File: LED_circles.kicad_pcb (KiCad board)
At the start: 2 copper layers, 125 x 125 mm, 134 parts, among them J1 Conn_ARM_SWD_EDGE, J2 USB4125-GF-A, U74 BD33GA3WEFJ, U75 M95256-WMN6P, U76 M95256-WMN6P, U77 STM32G071KBTxN

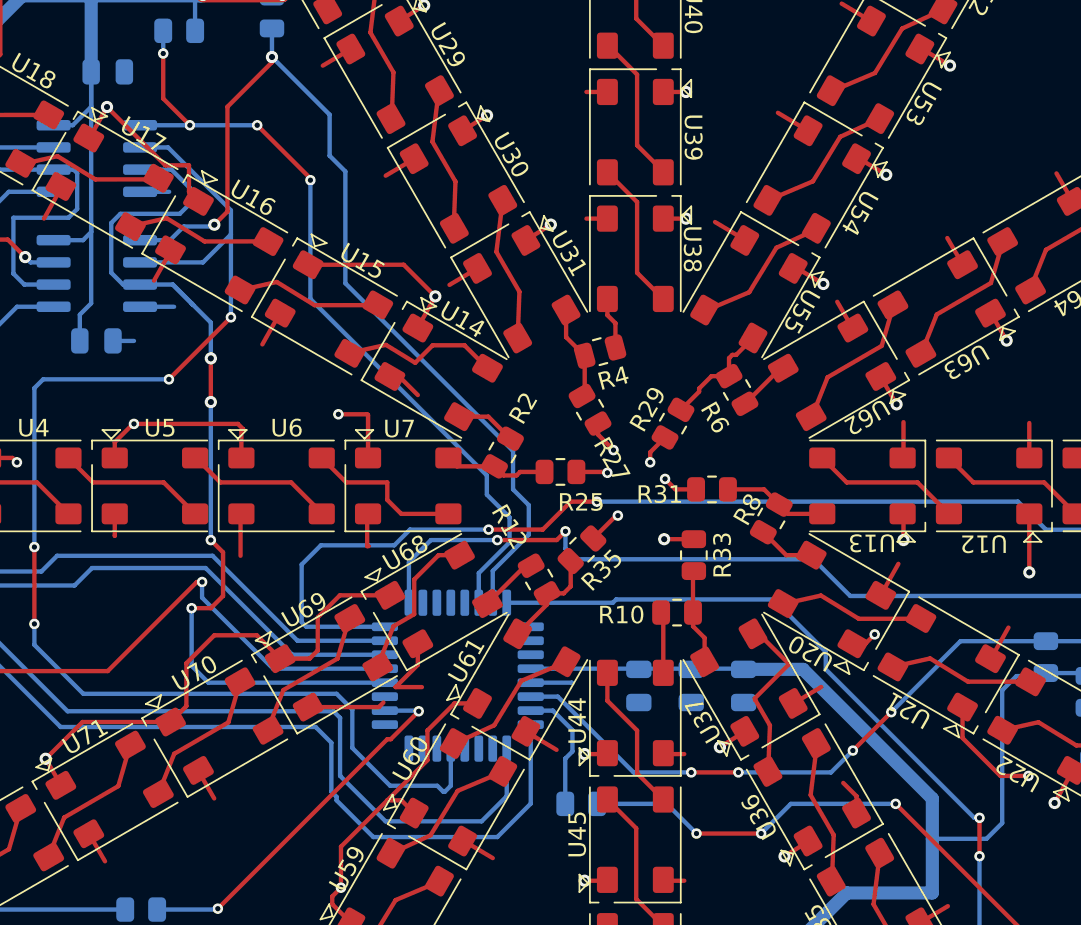
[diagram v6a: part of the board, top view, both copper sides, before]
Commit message: Fixed DRC issues
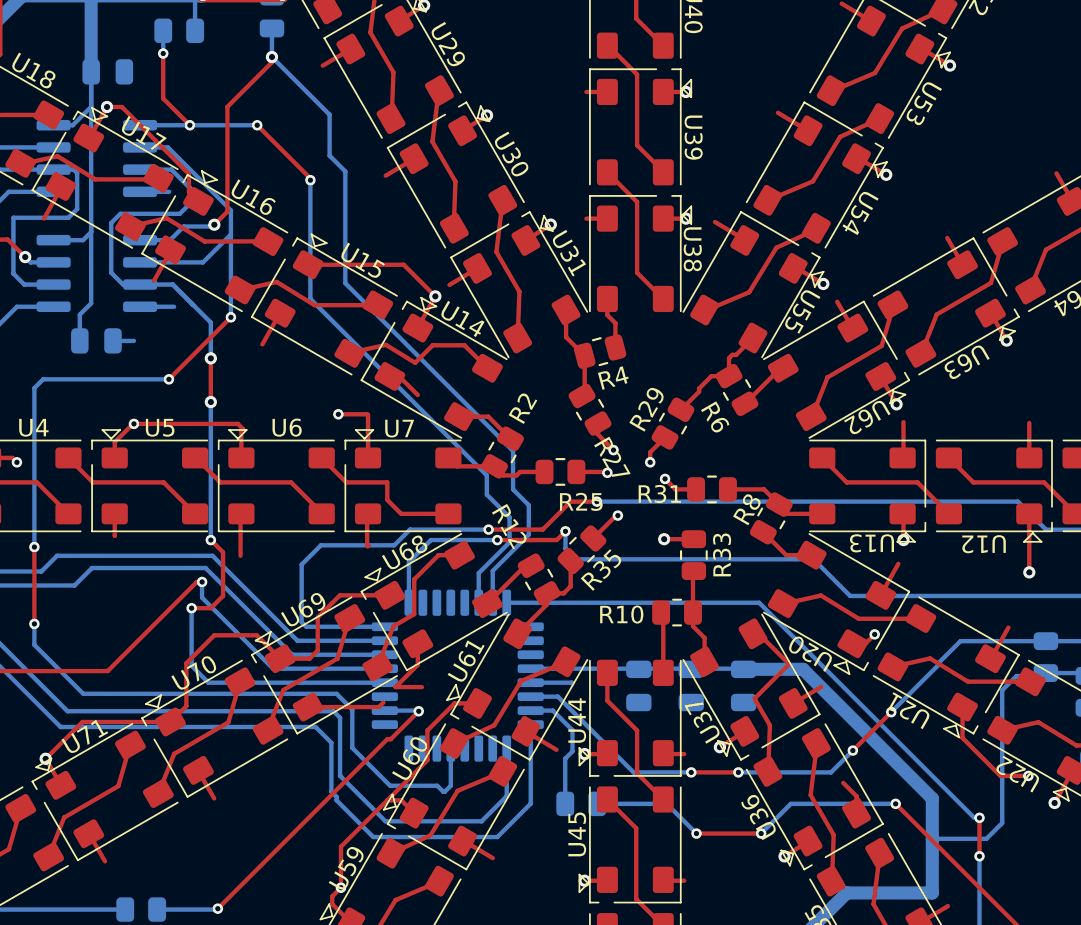
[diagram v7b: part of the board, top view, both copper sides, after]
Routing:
- net Net-(D1-A): track 106.8 -> 106.0 mm
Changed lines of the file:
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@@
-	)
-	(segment
-		(start 117.95 83.171916)
-		(end 117.95 81.65)
-		(width 0.25)
-		(layer "F.Cu")
-		(net 62)
 	)
 	(segment
@@
 	)
 	(segment
-		(start 116.595749 81.65)
-		(end 113.256391 78.310642)
-		(width 0.25)
-		(layer "F.Cu")
-		(net 62)
-	)
-	(segment
 		(start 160.628717 132.85)
 		(end 159.189358 133.756391)
@@
 	)
 	(segment
+		(start 113.256391 78.310642)
+		(end 114.110642 78.310642)
+		(width 0.25)
+		(layer "F.Cu")
+		(net 62)
+	)
+	(segment
 		(start 124.850642 109.889358)
 		(end 125.32 109.42)
@@
 	)
 	(segment
-		(start 118.492444 83.71436)
-		(end 117.95 83.171916)
-		(width 0.25)
-		(layer "F.Cu")
-		(net 62)
-	)
-	(segment
 		(start 99.2 98.4)
 		(end 99.2 96.55)
@@
 	)
 	(segment
-		(start 117.95 81.65)
-		(end 116.595749 81.65)
-		(width 0.25)
-		(layer "F.Cu")
-		(net 62)
-	)
-	(segment
 		(start 141.9 122.6)
 		(end 140.6 122.6)
@@
 	)
 	(segment
+		(start 117.95 83.171916)
+		(end 118.492444 83.71436)
+		(width 0.25)
+		(layer "F.Cu")
+		(net 62)
+	)
+	(segment
 		(start 141.85 99.2)
 		(end 141.9 99.25)
@@
 	)
 	(segment
+		(start 114.110642 78.310642)
+		(end 117.95 82.15)
+		(width 0.25)
+		(layer "F.Cu")
+		(net 62)
+	)
+	(segment
 		(start 145.1 84.7)
 		(end 146.4 84.7)
@@
 		(start 145.15 70.2)
 		(end 146.45 70.2)
+		(width 0.25)
+		(layer "F.Cu")
+		(net 62)
+	)
+	(segment
+		(start 117.95 82.15)
+		(end 117.95 83.171916)
 		(width 0.25)
 		(layer "F.Cu")
@@
 	)
 	(segment
-		(start 154.4 109.5)
-		(end 154.4 110.5)
+		(start 123 147.5)
+		(end 117.5 153)
+		(width 0.25)
+		(layer "B.Cu")
+		(net 63)
+	)
+	(segment
+		(start 118 157.5)
+		(end 118.05 157.55)
+		(width 0.25)
+		(layer "B.Cu")
+		(net 63)
+	)
+	(segment
+		(start 163.2 121.2)
+		(end 163.2 126.1)
+		(width 0.25)
+		(layer "B.Cu")
+		(net 63)
+	)
+	(segment
+		(start 118.05 157.55)
+		(end 121.4 157.55)
+		(width 0.25)
+		(layer "B.Cu")
+		(net 63)
+	)
+	(segment
+		(start 162.4 126.9)
+		(end 157.15056 126.9)
+		(width 0.25)
+		(layer "B.Cu")
+		(net 63)
+	)
+	(segment
+		(start 150.58795 106.68795)
+		(end 162.9 119)
+		(width 0.25)
+		(layer "B.Cu")
+		(net 63)
+	)
+	(segment
+		(start 163.2 126.1)
+		(end 162.4 126.9)
+		(width 0.25)
+		(layer "B.Cu")
+		(net 63)
+	)
+	(segment
+		(start 118 157)
+		(end 118 157.5)
+		(width 0.25)
+		(layer "B.Cu")
+		(net 63)
+	)
+	(segment
+		(start 117.5 156.5)
+		(end 118 157)
+		(width 0.25)
+		(layer "B.Cu")
+		(net 63)
+	)
+	(segment
+		(start 136.137104 106.68795)
+		(end 150.58795 106.68795)
 		(width 0.25)
 		(layer "B.Cu")
@@
 		(width 0.25)
 		(layer "B.Cu")
-		(net 63)
-	)
-	(segment
-		(start 142.4 106.5)
-		(end 151.4 106.5)
-		(width 0.25)
-		(layer "B.Cu")
-		(net 63)
-	)
-	(segment
-		(start 151.4 106.5)
-		(end 154.4 109.5)
-		(width 0.25)
-		(layer "B.Cu")
-		(net 63)
-	)
-	(segment
-		(start 123 147.5)
-		(end 117.5 153)
-		(width 0.25)
-		(layer "B.Cu")
-		(net 63)
-	)
-	(segment
-		(start 118 157.5)
-		(end 118.05 157.55)
-		(width 0.25)
-		(layer "B.Cu")
-		(net 63)
-	)
-	(segment
-		(start 136.137104 106.68795)
-		(end 142.21205 106.68795)
-		(width 0.25)
-		(layer "B.Cu")
-		(net 63)
-	)
-	(segment
-		(start 163.2 121.2)
-		(end 163.2 126.1)
-		(width 0.25)
-		(layer "B.Cu")
-		(net 63)
-	)
-	(segment
-		(start 118.05 157.55)
-		(end 121.4 157.55)
-		(width 0.25)
-		(layer "B.Cu")
-		(net 63)
-	)
-	(segment
-		(start 162.4 126.9)
-		(end 157.15056 126.9)
-		(width 0.25)
-		(layer "B.Cu")
-		(net 63)
-	)
-	(segment
-		(start 163.2 126.1)
-		(end 162.4 126.9)
-		(width 0.25)
-		(layer "B.Cu")
-		(net 63)
-	)
-	(segment
-		(start 118 157)
-		(end 118 157.5)
-		(width 0.25)
-		(layer "B.Cu")
-		(net 63)
-	)
-	(segment
-		(start 154.4 110.5)
-		(end 162.9 119)
-		(width 0.25)
-		(layer "B.Cu")
-		(net 63)
-	)
-	(segment
-		(start 117.5 156.5)
-		(end 118 157)
-		(width 0.25)
-		(layer "B.Cu")
-		(net 63)
-	)
-	(segment
-		(start 142.21205 106.68795)
-		(end 142.4 106.5)
-		(width 0.25)
-		(layer "B.Cu")
